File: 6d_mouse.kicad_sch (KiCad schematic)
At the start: 14 parts, among them J1 vik-module-connector, U1 TLV493D, U2 TLV493D, U3 SiP32431DR3

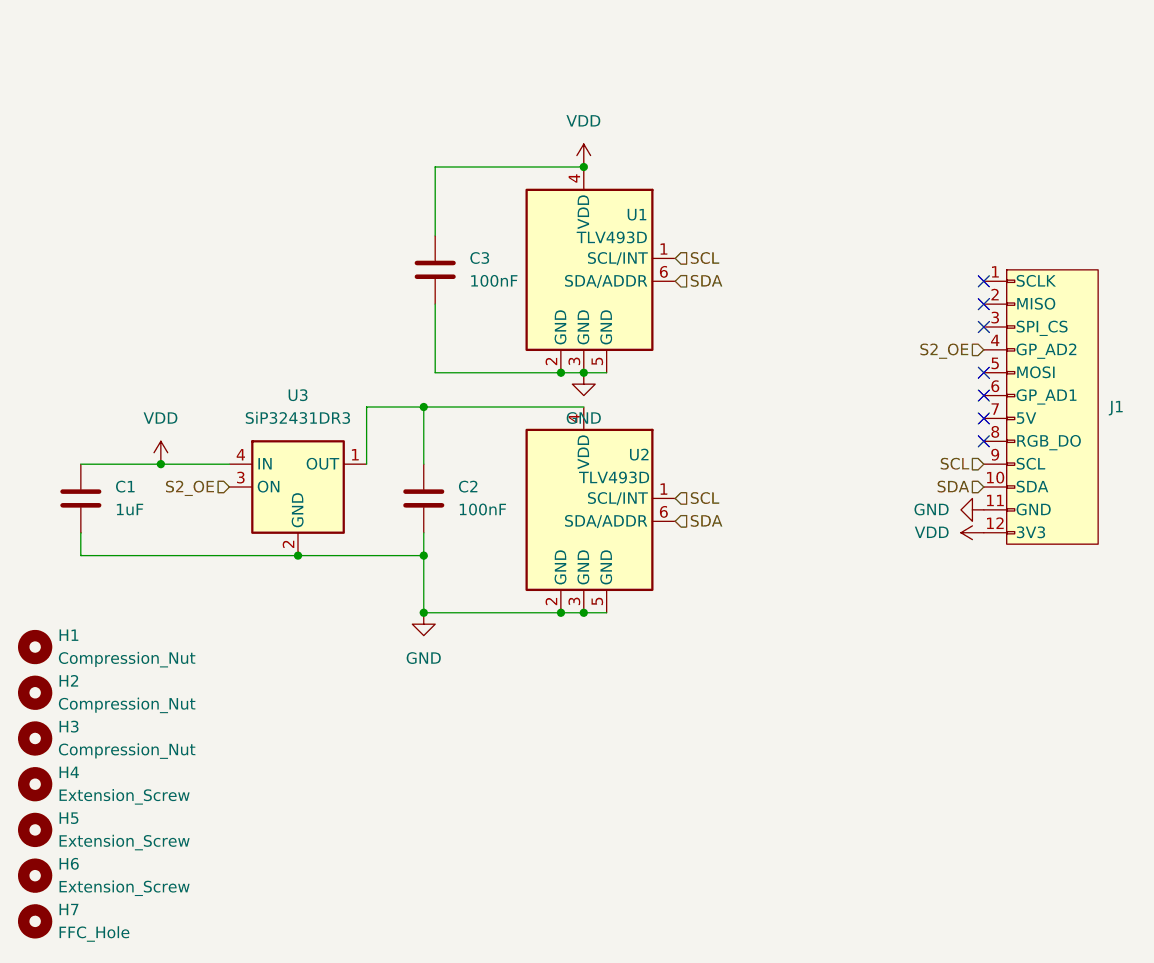
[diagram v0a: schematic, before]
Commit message: fixed missing registers for I2C
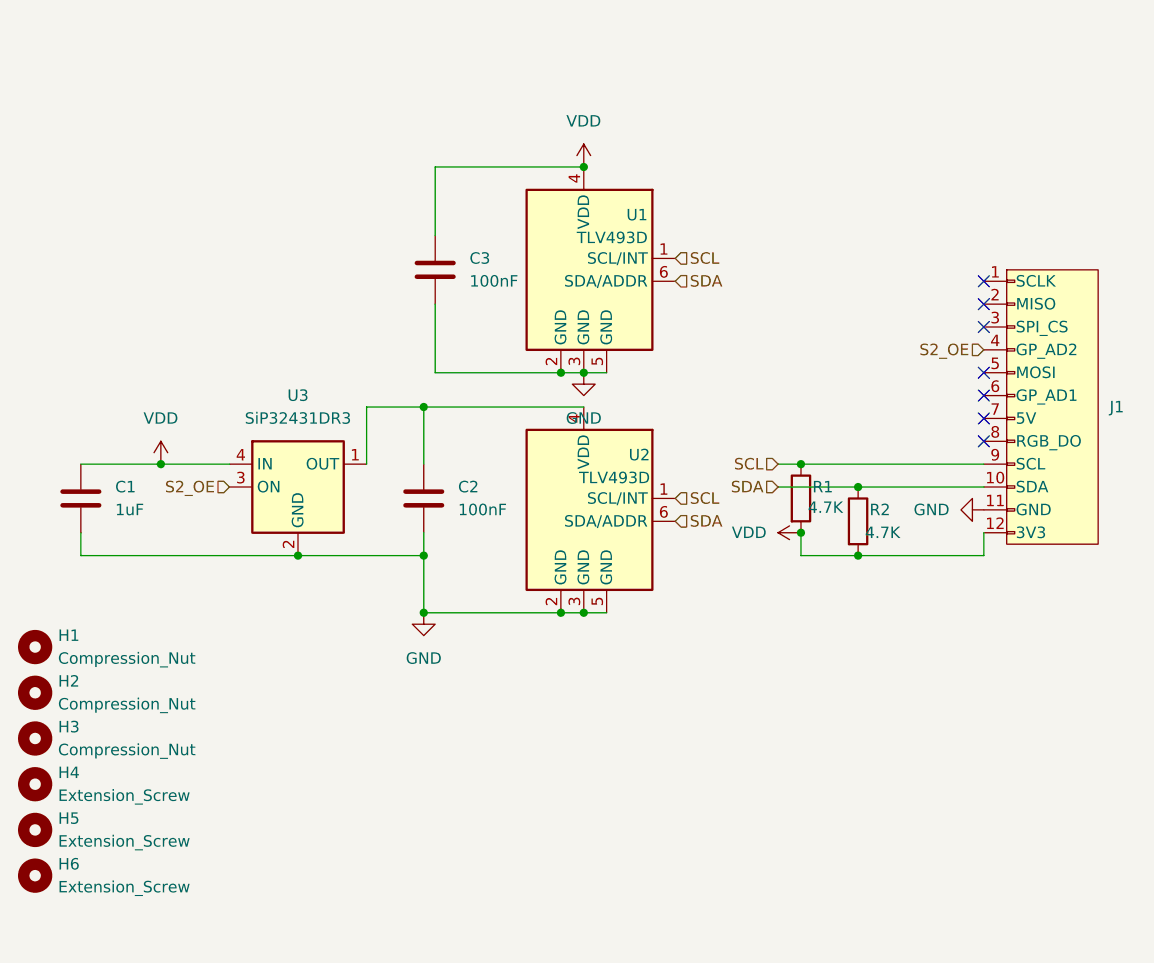
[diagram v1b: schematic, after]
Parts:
- removed H7: FFC_Hole, symbol Mechanical:MountingHole
- added R1, R2: 4.7K, Resistor_SMD:R_0603_1608Metric_Pad0.98x0.95mm_HandSolder, symbol Device:R
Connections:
- net SCL: now also R1.1
- net SDA: now also R2.1
- net VDD: now also R1.2, R2.2
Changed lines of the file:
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@@
+	)
+	(junction
+		(at 120.65 72.39)
+		(diameter 0)
+		(color 0 0 0 0)
 	)
 	(junction
@@
 	)
 	(junction
+		(at 127 74.93)
+		(diameter 0)
+		(color 0 0 0 0)
+	)
+	(junction
 		(at 78.74 74.93)
 		(diameter 0)
@@
 	)
 	(junction
+		(at 127 67.31)
+		(diameter 0)
+		(color 0 0 0 0)
+	)
+	(junction
 		(at 96.52 81.28)
 		(diameter 0)
 		(color 0 0 0 0)
 	)
+	(junction
+		(at 120.65 64.77)
+		(diameter 0)
+		(color 0 0 0 0)
+	)
 	(no_connect
 		(at 140.97 44.45)
@@
 	(wire
 		(pts
+			(xy 120.65 74.93) (xy 127 74.93)
+		)
+		(stroke
+			(width 0)
+			(type default)
+		)
+	)
+	(wire
+		(pts
 			(xy 49.53 64.77) (xy 57.15 64.77)
 		)
@@
 	(wire
 		(pts
+			(xy 118.11 67.31) (xy 127 67.31)
+		)
+		(stroke
+			(width 0)
+			(type default)
+		)
+	)
+	(wire
+		(pts
 			(xy 78.74 81.28) (xy 93.98 81.28)
 		)
@@
 	(wire
 		(pts
+			(xy 127 67.31) (xy 140.97 67.31)
+		)
+		(stroke
+			(width 0)
+			(type default)
+		)
+	)
+	(wire
+		(pts
 			(xy 40.64 74.93) (xy 64.77 74.93)
 		)
@@
 	(wire
 		(pts
+			(xy 120.65 64.77) (xy 140.97 64.77)
+		)
+		(stroke
+			(width 0)
+			(type default)
+		)
+	)
+	(wire
+		(pts
 			(xy 40.64 72.39) (xy 40.64 74.93)
 		)
@@
 	(wire
 		(pts
+			(xy 140.97 74.93) (xy 140.97 72.39)
+		)
+		(stroke
+			(width 0)
+			(type default)
+		)
+	)
+	(wire
+		(pts
 			(xy 80.01 31.75) (xy 96.52 31.75)
 		)
@@
 	(wire
 		(pts
+			(xy 140.97 74.93) (xy 127 74.93)
+		)
+		(stroke
+			(width 0)
+			(type default)
+		)
+	)
+	(wire
+		(pts
+			(xy 118.11 64.77) (xy 120.65 64.77)
+		)
+		(stroke
+			(width 0)
+			(type default)
+		)
+	)
+	(wire
+		(pts
 			(xy 78.74 58.42) (xy 96.52 58.42)
 		)
@@
 		(pts
 			(xy 80.01 54.61) (xy 93.98 54.61)
+		)
+		(stroke
+			(width 0)
+			(type default)
+		)
+	)
+	(wire
+		(pts
+			(xy 120.65 72.39) (xy 120.65 74.93)
 		)
 		(stroke
@@
 	(hierarchical_label "SDA"
 		(shape input)
-		(at 140.97 67.31 180)
+		(at 118.11 67.31 180)
 		(fields_autoplaced yes)
 		(effects
@@
 	(hierarchical_label "SCL"
 		(shape input)
-		(at 140.97 64.77 180)
+		(at 118.11 64.77 180)
 		(fields_autoplaced yes)
 		(effects
@@
 	)
 	(symbol
+		(lib_id "Device:R")
+		(at 120.65 68.58 0)
+		(unit 1)
+		(exclude_from_sim no)
+		(in_bom yes)
+		(on_board yes)
+		(dnp no)
+		(property "Reference" "R1"
+			(at 121.92 67.31 0)
+			(effects
+				(font
+					(size 1.27 1.27)
+				)
+				(justify left)
+			)
+		)
+		(property "Value" "4.7K"
+			(at 121.412 69.596 0)
+			(effects
+				(font
+					(size 1.27 1.27)
+				)
+				(justify left)
+			)
+		)
+		(property "Footprint" "Resistor_SMD:R_0603_1608Metric_Pad0.98x0.95mm_HandSolder"
+			(at 118.872 68.58 90)
+			(effects
+				(font
+					(size 1.27 1.27)
+				)
+				(hide yes)
+			)
+		)
+		(property "Datasheet" "~"
+			(at 120.65 68.58 0)
+			(effects
+				(font
+					(size 1.27 1.27)
+				)
+				(hide yes)
+			)
+		)
+		(property "Description" "Resistor"
+			(at 120.65 68.58 0)
+			(effects
+				(font
+					(size 1.27 1.27)
+				)
+				(hide yes)
+			)
+		)
+		(pin "1"
+		)
+		(pin "2"
+		)
+		(instances
+			(project "6d_mouse"
+				(path "/86a2bcde-12ae-4cd8-a215-c4728955bebf"
+					(reference "R1")
+					(unit 1)
+				)
+			)
+		)
+	)
+	(symbol
 		(lib_id "power:GND")
 		(at 78.74 81.28 0)
@@
 	)
 	(symbol
+		(lib_id "Device:R")
+		(at 127 71.12 0)
+		(unit 1)
+		(exclude_from_sim no)
+		(in_bom yes)
+		(on_board yes)
+		(dnp no)
+		(property "Reference" "R2"
+			(at 128.27 69.85 0)
+			(effects
+				(font
+					(size 1.27 1.27)
+				)
+				(justify left)
+			)
+		)
+		(property "Value" "4.7K"
+			(at 127.762 72.39 0)
+			(effects
+				(font
+					(size 1.27 1.27)
+				)
+				(justify left)
+			)
+		)
+		(property "Footprint" "Resistor_SMD:R_0603_1608Metric_Pad0.98x0.95mm_HandSolder"
+			(at 125.222 71.12 90)
+			(effects
+				(font
+					(size 1.27 1.27)
+				)
+				(hide yes)
+			)
+		)
+		(property "Datasheet" "~"
+			(at 127 71.12 0)
+			(effects
+				(font
+					(size 1.27 1.27)
+				)
+				(hide yes)
+			)
+		)
+		(property "Description" "Resistor"
+			(at 127 71.12 0)
+			(effects
+				(font
+					(size 1.27 1.27)
+				)
+				(hide yes)
+			)
+		)
+		(pin "1"
+		)
+		(pin "2"
+		)
+		(instances
+			(project "6d_mouse"
+				(path "/86a2bcde-12ae-4cd8-a215-c4728955bebf"
+					(reference "R2")
+					(unit 1)
+				)
+			)
+		)
+	)
+	(symbol
 		(lib_id "Device:C")
 		(at 78.74 68.58 0)
@@
 				(path "/86a2bcde-12ae-4cd8-a215-c4728955bebf"
 					(reference "U3")
-					(unit 1)
-				)
-			)
-		)
-	)
-	(symbol
-		(lib_id "Mechanical:MountingHole")
-		(at 35.56 115.57 0)
-		(unit 1)
-		(exclude_from_sim yes)
-		(in_bom no)
-		(on_board yes)
-		(dnp no)
-		(fields_autoplaced yes)
-		(property "Reference" "H7"
-			(at 38.1 114.2999 0)
-			(effects
-				(font
-					(size 1.27 1.27)
-				)
-				(justify left)
-			)
-		)
-		(property "Value" "FFC_Hole"
-			(at 38.1 116.8399 0)
-			(effects
-				(font
-					(size 1.27 1.27)
-				)
-				(justify left)
-			)
-		)
-		(property "Footprint" ""
-			(at 35.56 115.57 0)
-			(effects
-				(font
-					(size 1.27 1.27)
-				)
-				(hide yes)
-			)
-		)
-		(property "Datasheet" "~"
-			(at 35.56 115.57 0)
-			(effects
-				(font
-					(size 1.27 1.27)
-				)
-				(hide yes)
-			)
-		)
-		(property "Description" "Mounting Hole without connection"
-			(at 35.56 115.57 0)
-			(effects
-				(font
-					(size 1.27 1.27)
-				)
-				(hide yes)
-			)
-		)
-		(instances
-			(project "6d_mouse"
-				(path "/86a2bcde-12ae-4cd8-a215-c4728955bebf"
-					(reference "H7")
 					(unit 1)
 				)
@@
 	(symbol
 		(lib_id "power:VDD")
-		(at 140.97 72.39 90)
+		(at 120.65 72.39 90)
 		(unit 1)
 		(exclude_from_sim no)
@@
 		(fields_autoplaced yes)
 		(property "Reference" "#PWR03"
-			(at 144.78 72.39 0)
+			(at 124.46 72.39 0)
 			(effects
 				(font
@@
 		)
 		(property "Value" "VDD"
-			(at 137.16 72.3899 90)
+			(at 116.84 72.3899 90)
 			(effects
 				(font
@@
 		)
 		(property "Footprint" ""
-			(at 140.97 72.39 0)
+			(at 120.65 72.39 0)
 			(effects
 				(font
@@
 		)
 		(property "Datasheet" ""
-			(at 140.97 72.39 0)
+			(at 120.65 72.39 0)
 			(effects
 				(font
@@
 		)
 		(property "Description" "Power symbol creates a global label with name \"VDD\""
-			(at 140.97 72.39 0)
-			(effects
-				(font
+			(at 120.65 72.39 0)
+			(effects
+				(font

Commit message: changed to TMAG5273
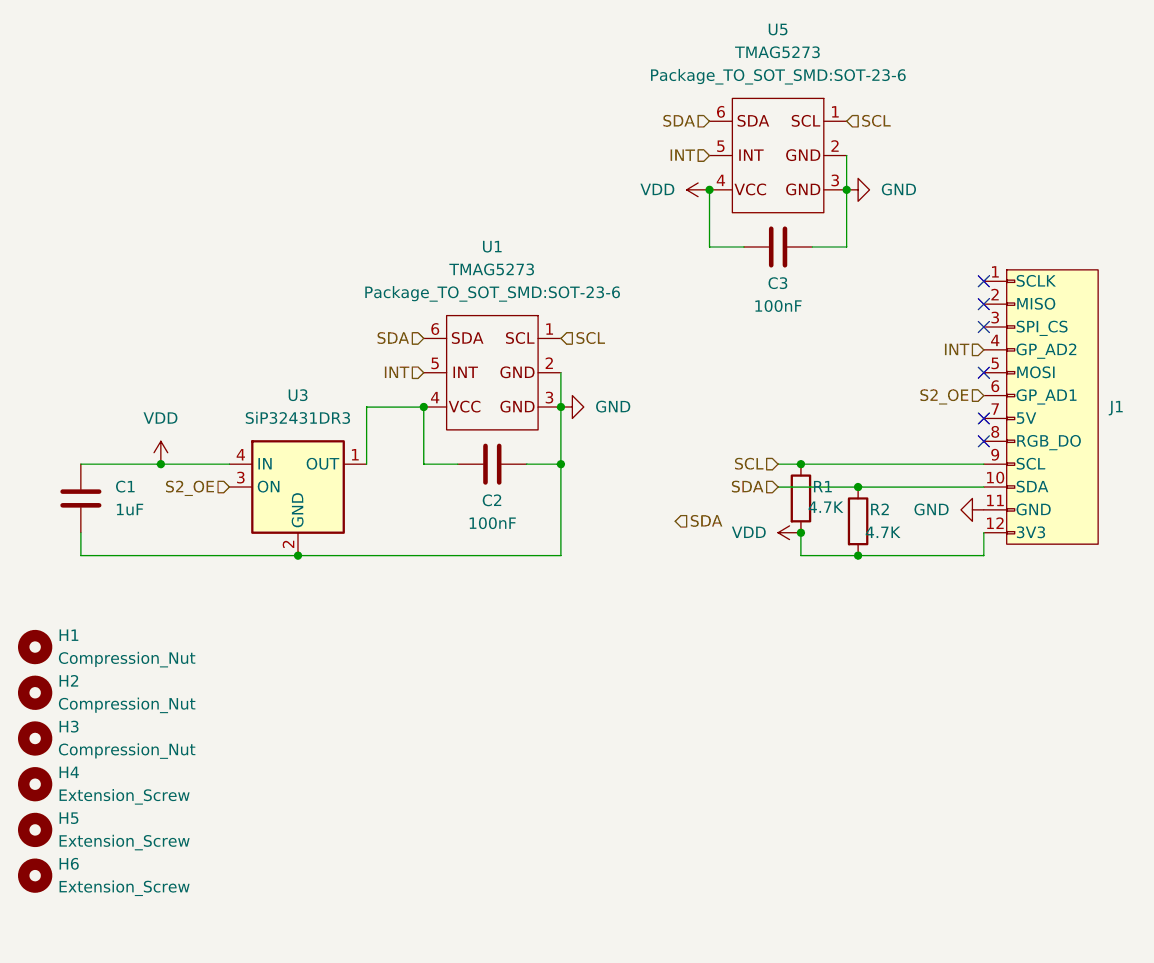
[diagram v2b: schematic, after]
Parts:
- removed U1, U2: TLV493D, Package_TO_SOT_SMD:SOT-23-6, symbol Sensor_Magnetic:TLV493D
- added U1, U5: TMAG5273, Package_TO_SOT_SMD:SOT-23-6, symbol vik:TMAG5273
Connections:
- net GND: now also U1.2 (GND), U1.3 (GND), U5.2 (GND), U5.3 (GND)
- net S2_OE: now also J1.6 (GP_AD1); no longer J1.4 (GP_AD2)
- net SCL: now also U1.1 (SCL), U5.1 (SCL)
- net SDA: now also U1.6 (SDA), U5.6 (SDA)
- net VDD: now also U5.4 (VCC)
- net at C2.1, U3.1 (OUT): now also U1.4 (VCC)
- new net INT: J1.4 (GP_AD2), U1.5 (INT), U5.5 (INT)
- no-connect marks 7 -> 6
